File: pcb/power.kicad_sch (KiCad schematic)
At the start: 34 parts, among them J2 USB_C_Top, J3 USB_C_Bottom, Q2 AO3401A, Q5 AO3400A, U2 TPS63000, U3 TPS63000, U4 TP4056

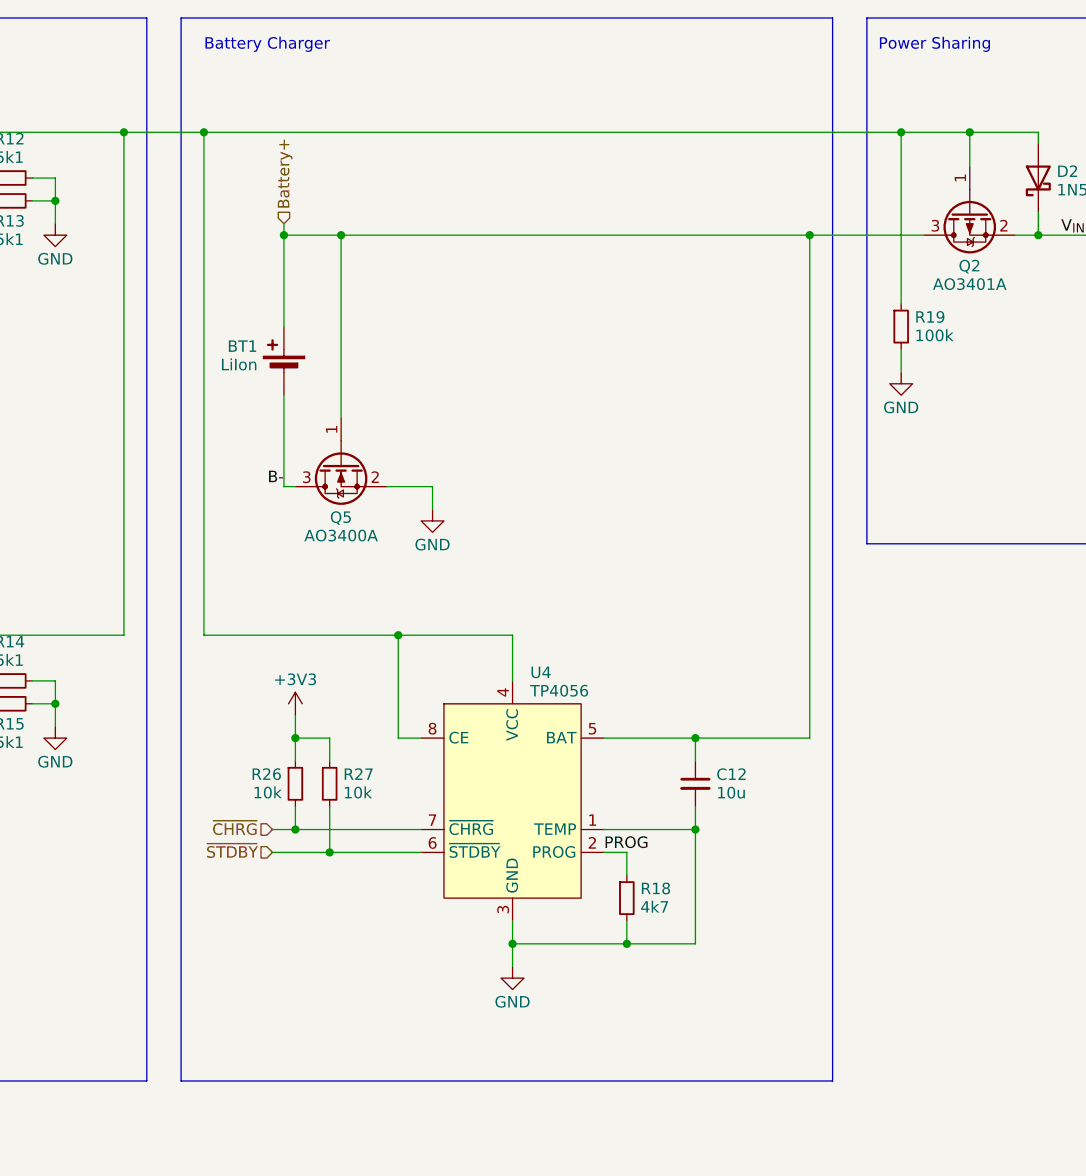
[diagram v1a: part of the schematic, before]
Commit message: feat: add disable jumper for battery charger
Adding a jumper to disable the TP4056 Battery Charger IC in case no battery is connected and the device is powered by USB only. No need for the IC to draw power in that case.
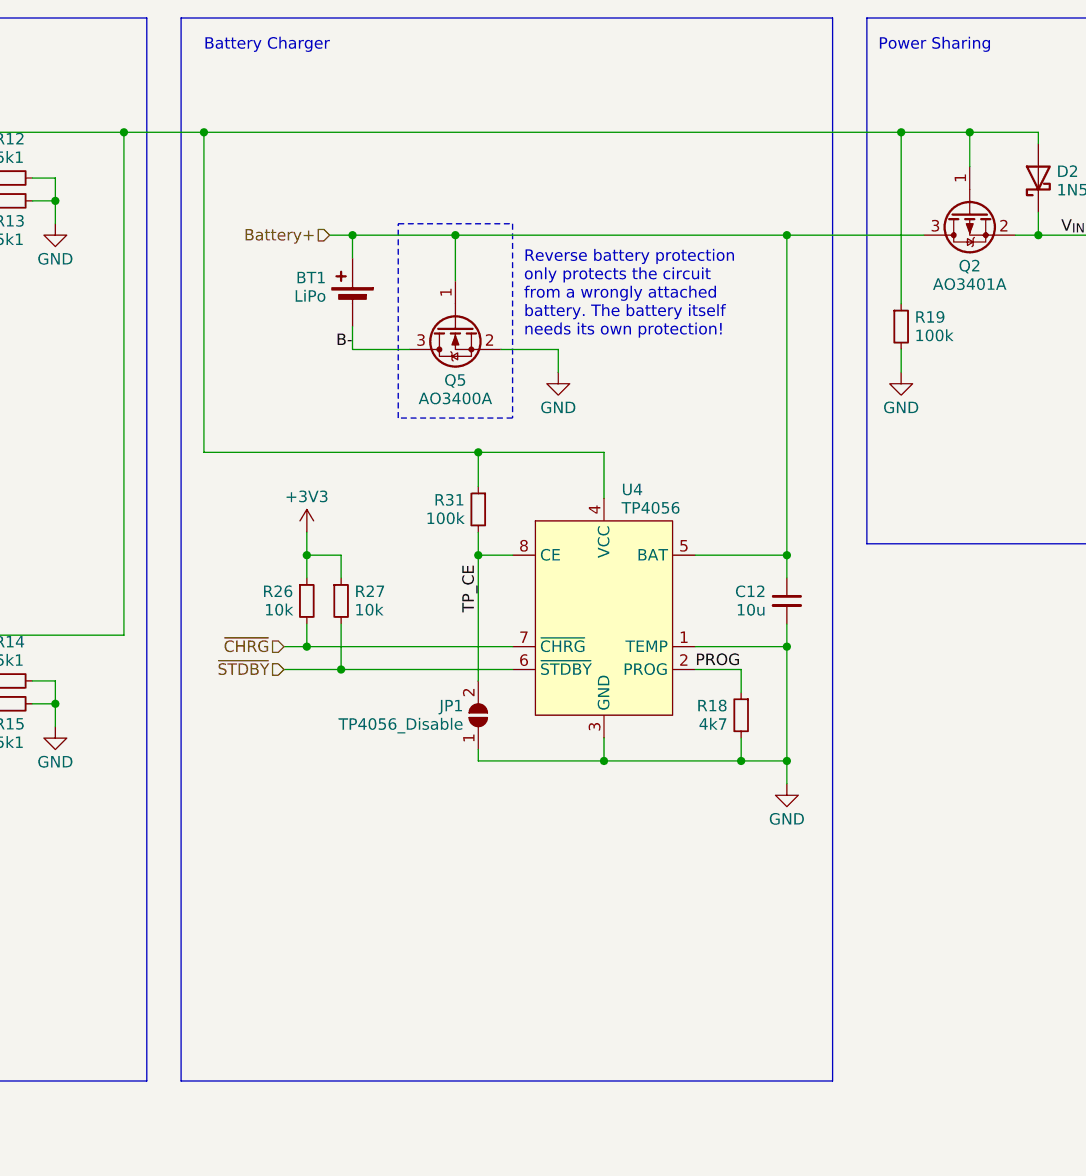
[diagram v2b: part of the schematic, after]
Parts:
- added JP1: TP4056_Disable, Jumper:SolderJumper-2_P1.3mm_Open_RoundedPad1.0x1.5mm, symbol Jumper:SolderJumper_2_Open
- added R31: 100k, Resistor_SMD:R_0402_1005Metric, symbol Device:R_Small
- BT1: value LiIon -> LiPo
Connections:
- net GND: now also JP1.1 (A)
- net V_{BUS}: now also R31.1; no longer U4.8 (CE)
- new net TP_CE: JP1.2 (B), R31.2, U4.8 (CE)
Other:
- note added: "Reverse battery protection only protects the circuit from a wrongly attached battery. The battery itself needs its own protection!"
- moved on the sheet: BT1, C12, Q5, R18, R26, R27, U4

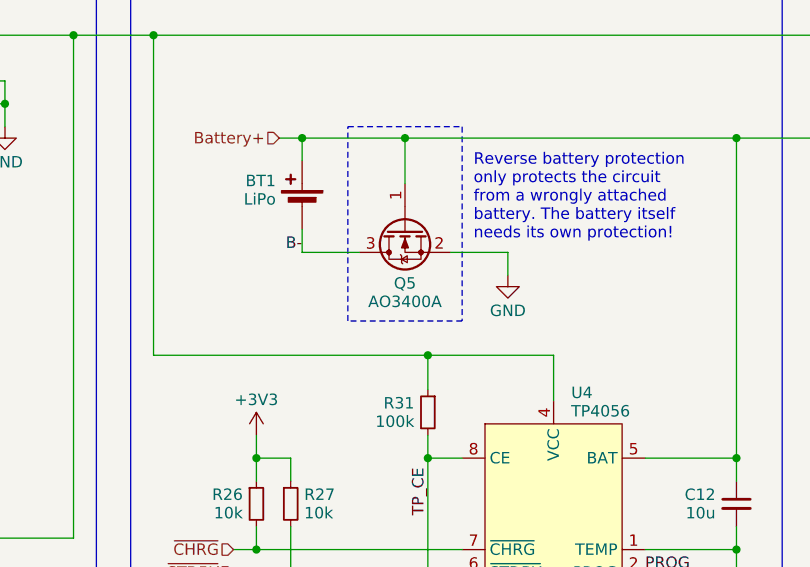
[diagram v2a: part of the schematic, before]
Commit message: feat: add more ways to wake up
Adding simple MOSFET logic to watch 4 signals for waking up from deep sleep
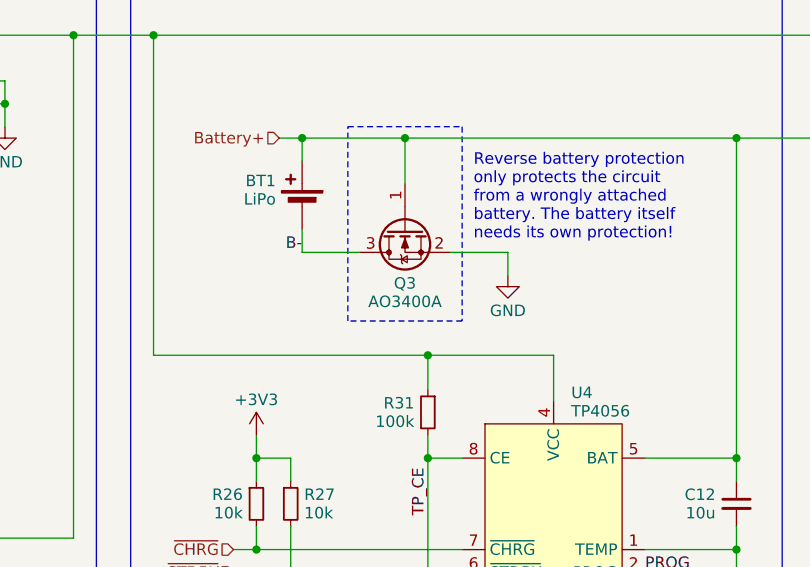
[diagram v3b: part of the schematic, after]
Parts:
- renumbered Q5 to Q3
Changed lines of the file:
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@@
   (symbol (lib_id "Transistor_FET:AO3400A") (at 113.03 59.69 90) (mirror x) (unit 1)
     (in_bom yes) (on_board yes) (dnp no)
-    (property "Reference" "Q5" (at 113.03 65.667 90)
+    (property "Reference" "Q3" (at 113.03 65.667 90)
       (effects (font (size 1.27 1.27)))
     )
@@
       (project "AC-Controller"
         (path "/a9b77c2b-ed0c-4412-867d-4d65898d0fc4/dbf41f99-e34f-4894-8335-e67b95846d1b"
-          (reference "Q5") (unit 1)
+          (reference "Q3") (unit 1)
         )
       )

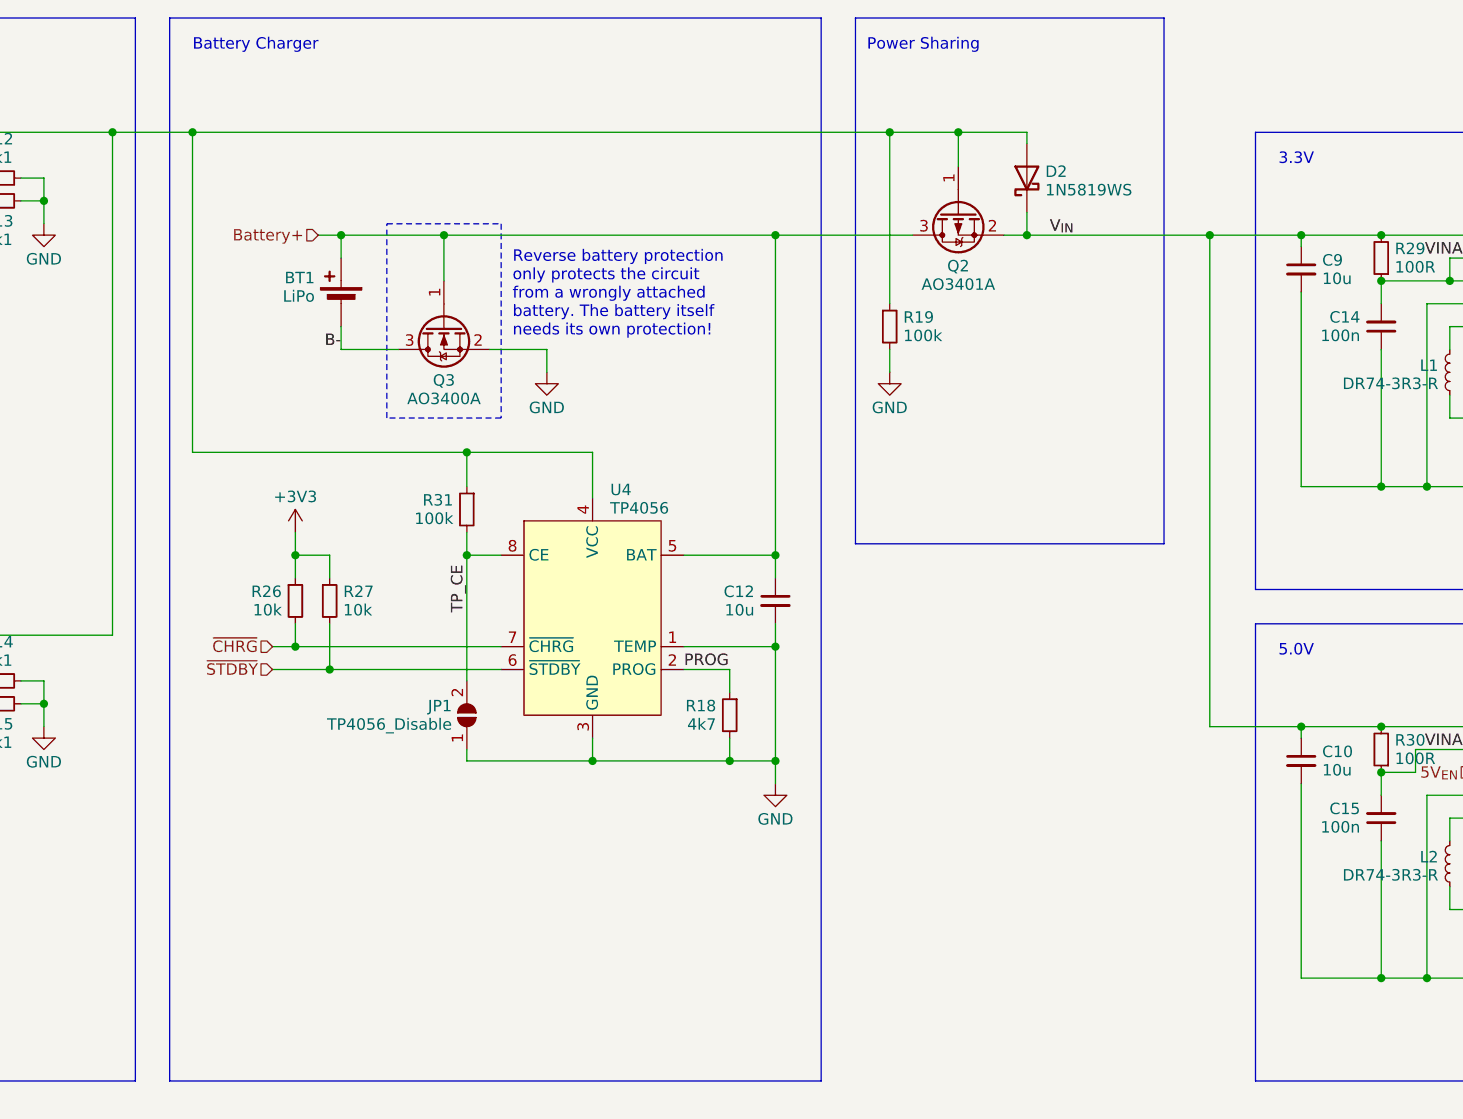
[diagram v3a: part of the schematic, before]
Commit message: feat: add power switch
Add switch to disconnect battery power from the circuit for when the device is not in use for a long time and reduce power consumption to a few nA
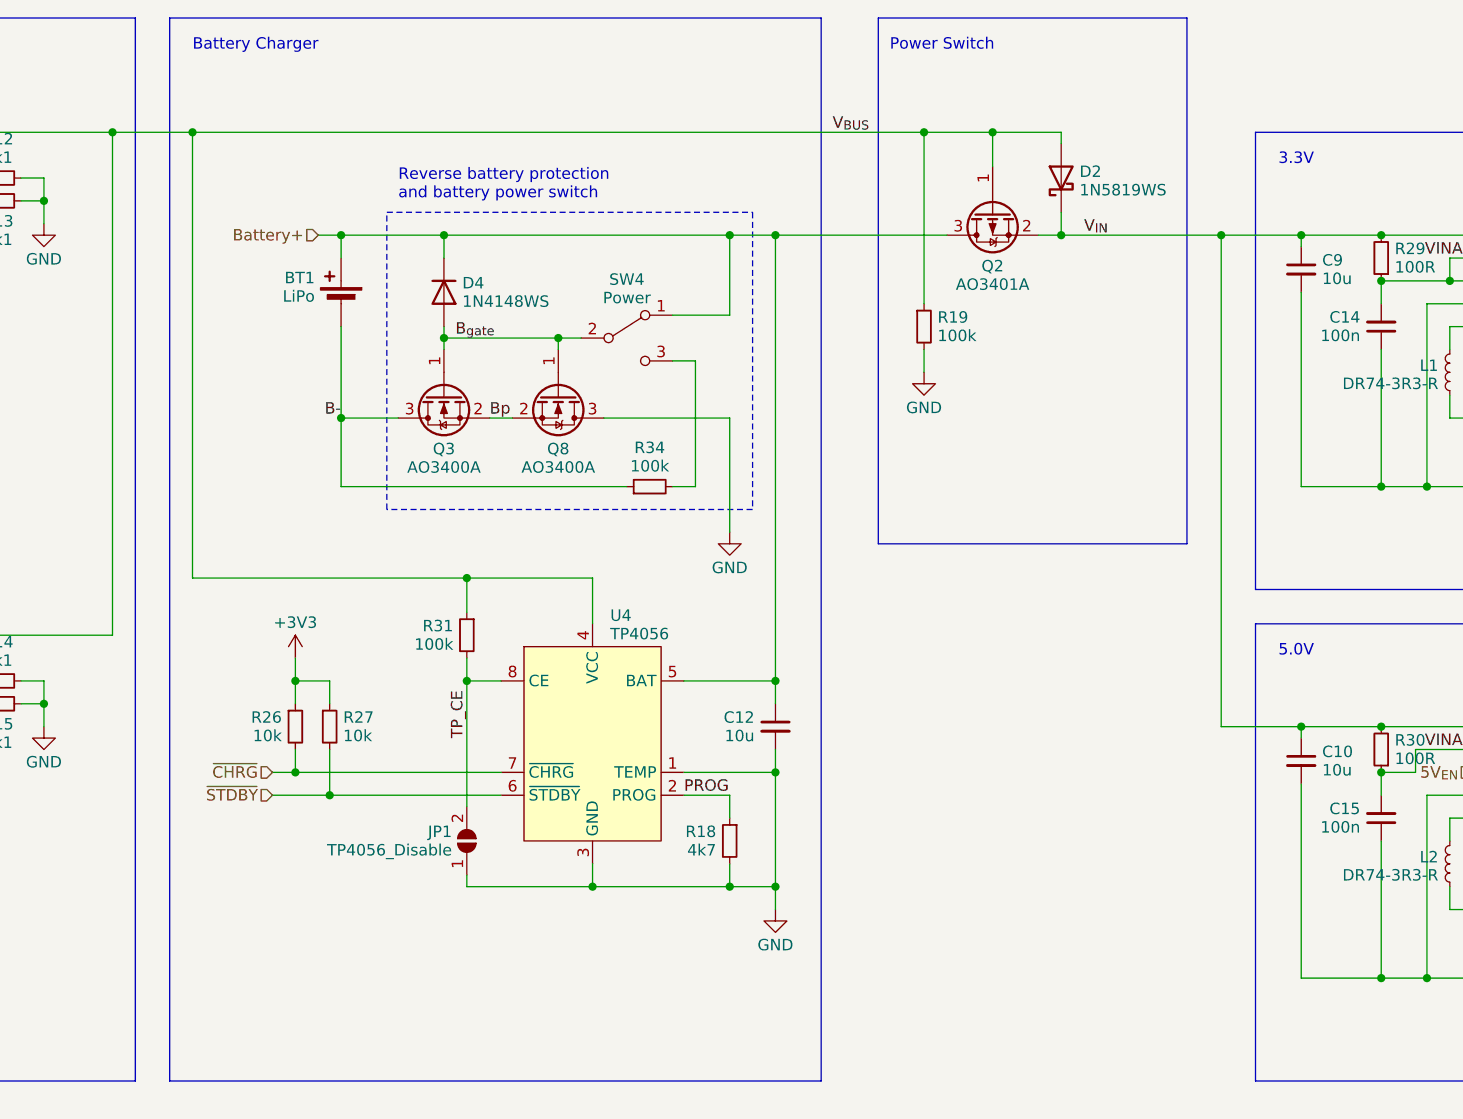
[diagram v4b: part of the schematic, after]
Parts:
- added D4: 1N4148WS, Diode_SMD:D_SOD-323, symbol Diode:1N4148WS
- added Q8: AO3400A, Package_TO_SOT_SMD:SOT-23, symbol Transistor_FET:AO3400A
- added R34: 100k, Resistor_SMD:R_0402_1005Metric, symbol Device:R_Small
- added SW4: Power, Button_Switch_SMD:SW_SPDT_PCM12, symbol Switch:SW_SPDT
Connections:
- net B-: now also R34.1
- net Battery+: now also D4.1 (K), SW4.1 (A); no longer Q3.1 (G)
- net GND: now also Q8.3 (D); no longer Q3.2 (S)
- new net: R34.2, SW4.3 (C)
- new net B_{gate}: D4.2 (A), Q3.1 (G), Q8.1 (G), SW4.2 (B)
- new net Bp: Q3.2 (S), Q8.2 (S)
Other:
- note added: "Power Switch"
- note added: "Reverse battery protection and battery power switch"
- note removed: "Power Sharing"
- note removed: "Reverse battery protection only protects the circuit from a wrongly attached battery. The battery itself needs its own protection!"
- moved on the sheet: C12, D2, JP1, Q2, Q3, R18, R19, R26, R27, R31, U4

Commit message: style: cleanup
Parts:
- renumbered Q8 to Q4
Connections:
- net B_{dis}: now reaches R34.2, SW4.3 (C)
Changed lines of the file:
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@@
+    (effects (font (size 1.27 1.27)) (justify left bottom))
+  )
+  (label "B_{dis}" (at 138.43 63.5 0) (fields_autoplaced)
     (effects (font (size 1.27 1.27)) (justify left bottom))
   )
@@
   (symbol (lib_id "Transistor_FET:AO3400A") (at 125.73 67.31 270) (unit 1)
     (in_bom yes) (on_board yes) (dnp no)
-    (property "Reference" "Q8" (at 125.73 73.287 90)
+    (property "Reference" "Q4" (at 125.73 73.287 90)
       (effects (font (size 1.27 1.27)))
     )
@@
       (project "AC-Controller"
         (path "/a9b77c2b-ed0c-4412-867d-4d65898d0fc4/dbf41f99-e34f-4894-8335-e67b95846d1b"
-          (reference "Q8") (unit 1)
-        )
-      )
+          (reference "Q4") (unit 1)
+        )
+      )

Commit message: fix: add missing part numbers
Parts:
- D4: LCSC (none) -> C2128
- SW4: LCSC (none) -> C221841
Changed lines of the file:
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@@
+      (effects (font (size 1.27 1.27)) hide)
+    )
+    (property "LCSC" "C2128" (at 113.03 55.88 0)
       (effects (font (size 1.27 1.27)) hide)
     )
@@
       (effects (font (size 1.27 1.27)) hide)
     )
+    (property "LCSC" "C221841" (at 133.35 60.96 0)
+      (effects (font (size 1.27 1.27)) hide)
+    )
